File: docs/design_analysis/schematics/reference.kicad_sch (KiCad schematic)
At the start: 0 parts

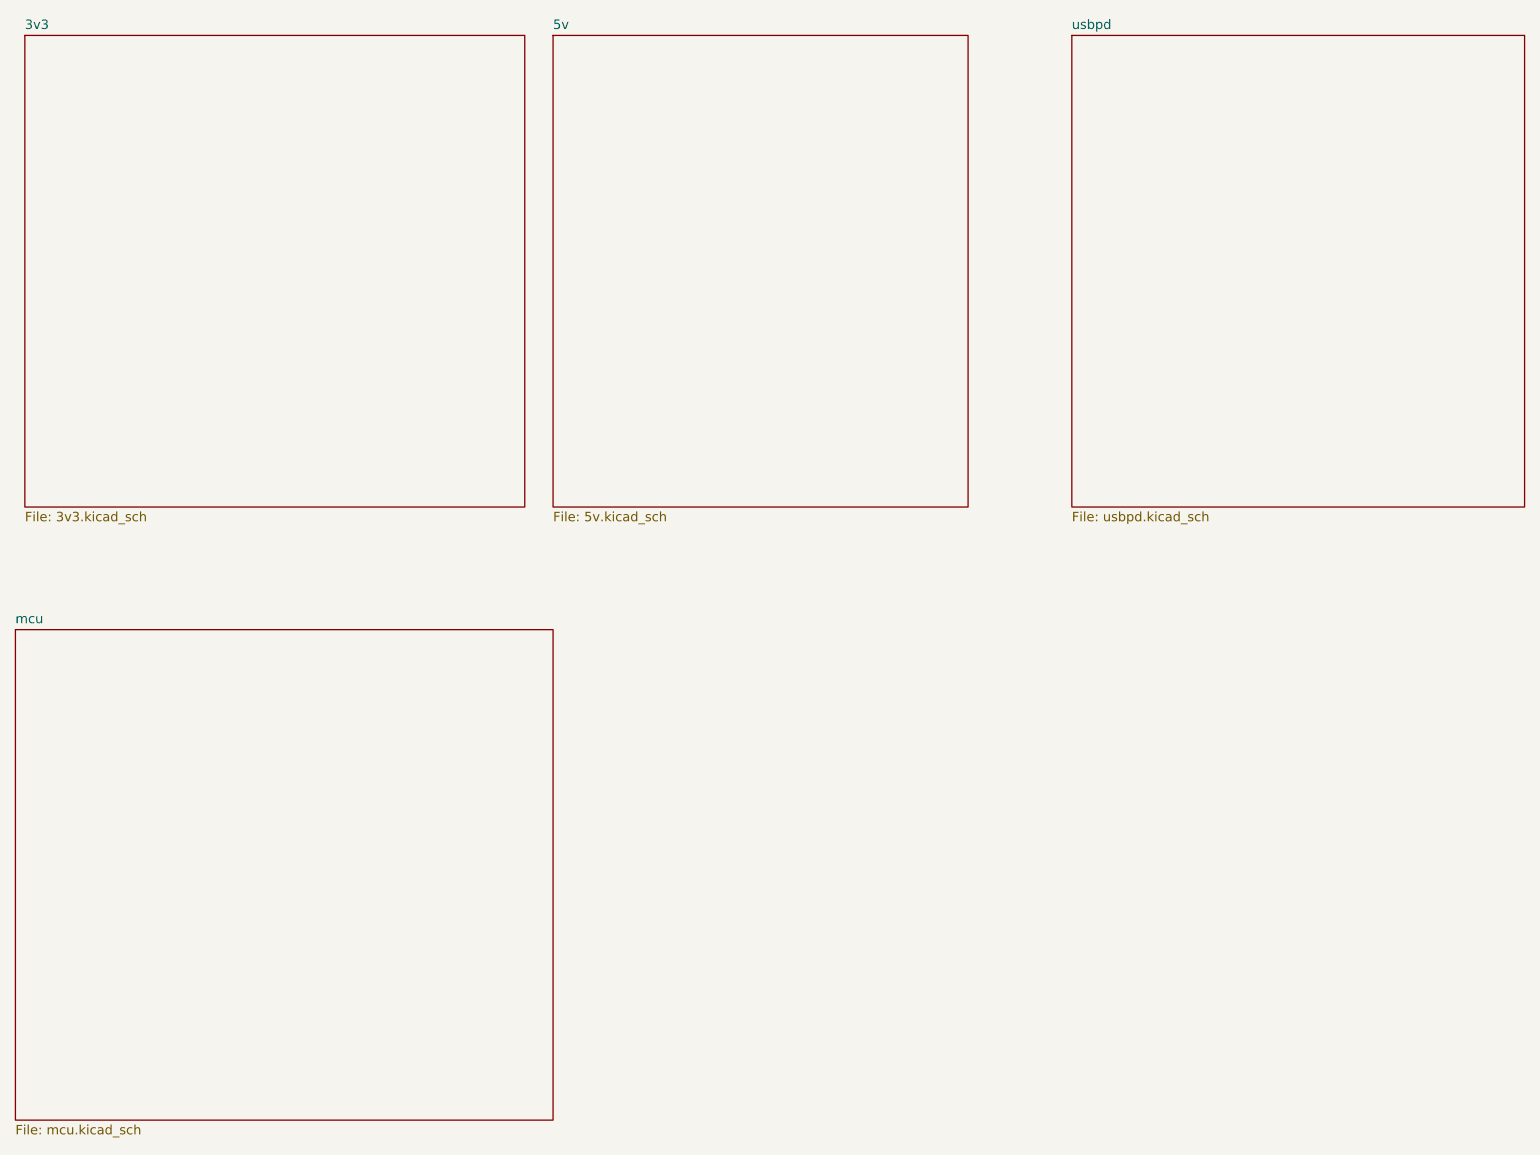
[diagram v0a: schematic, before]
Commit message: HV converter Rev C redesign around LM5156
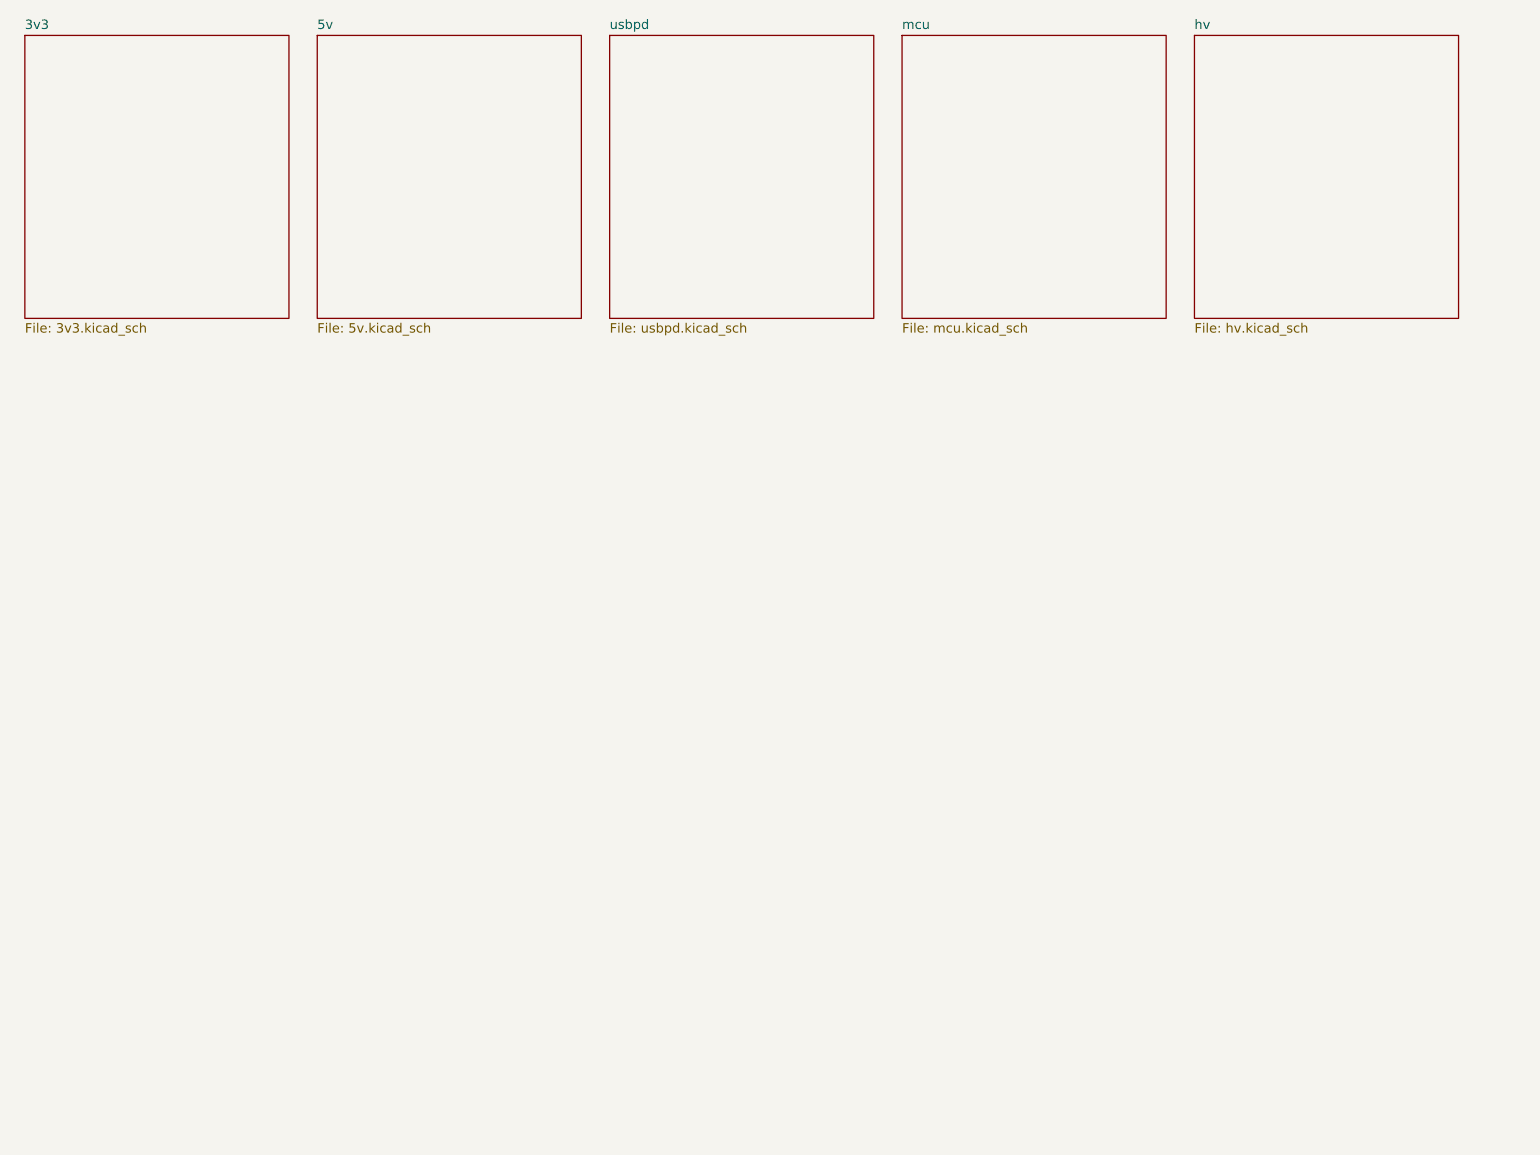
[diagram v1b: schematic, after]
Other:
- added sheet hv (hv.kicad_sch)
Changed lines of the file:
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@@
 (kicad_sch
-	(version 20250114)
+	(version 20260306)
 	(generator "eeschema")
-	(generator_version "9.0")
+	(generator_version "10.0")
 	(paper "A4")
 	(sheet
-		(at 99.06 24.13)
-		(size 55.88 63.5)
-		(exclude_from_sim no)
-		(in_bom yes)
-		(on_board yes)
-		(dnp no)
-		(fields_autoplaced yes)
-		(stroke
-			(width 0.1524)
-			(type solid)
-		)
-		(fill
-			(color 0 0 0 0.0000)
+		(at 67.31 24.13)
+		(size 35.56 38.1)
+		(exclude_from_sim no)
+		(in_bom yes)
+		(on_board yes)
+		(dnp no)
+		(fields_autoplaced yes)
+		(stroke
+			(width 0.1524)
+			(type solid)
+		)
+		(fill
+			(color 0 0 0 0)
 		)
 		(property "Sheetname" "5v"
-			(at 99.06 23.4184 0)
+			(at 67.31 23.4184 0)
+			(show_name no)
+			(do_not_autoplace no)
 			(effects
 				(font
@@
 		)
 		(property "Sheetfile" "5v.kicad_sch"
-			(at 99.06 88.2146 0)
+			(at 67.31 62.8146 0)
+			(show_name no)
+			(do_not_autoplace no)
 			(effects
 				(font
@@
 	(sheet
 		(at 27.94 24.13)
-		(size 67.31 63.5)
-		(exclude_from_sim no)
-		(in_bom yes)
-		(on_board yes)
-		(dnp no)
-		(fields_autoplaced yes)
-		(stroke
-			(width 0.1524)
-			(type solid)
-		)
-		(fill
-			(color 0 0 0 0.0000)
+		(size 35.56 38.1)
+		(exclude_from_sim no)
+		(in_bom yes)
+		(on_board yes)
+		(dnp no)
+		(fields_autoplaced yes)
+		(stroke
+			(width 0.1524)
+			(type solid)
+		)
+		(fill
+			(color 0 0 0 0)
 		)
 		(property "Sheetname" "3v3"
 			(at 27.94 23.4184 0)
+			(show_name no)
+			(do_not_autoplace no)
 			(effects
 				(font
@@
 		)
 		(property "Sheetfile" "3v3.kicad_sch"
-			(at 27.94 88.2146 0)
+			(at 27.94 62.8146 0)
+			(show_name no)
+			(do_not_autoplace no)
 			(effects
 				(font
@@
 	)
 	(sheet
-		(at 26.67 104.14)
-		(size 72.39 66.04)
-		(exclude_from_sim no)
-		(in_bom yes)
-		(on_board yes)
-		(dnp no)
-		(fields_autoplaced yes)
-		(stroke
-			(width 0.1524)
-			(type solid)
-		)
-		(fill
-			(color 0 0 0 0.0000)
+		(at 146.05 24.13)
+		(size 35.56 38.1)
+		(exclude_from_sim no)
+		(in_bom yes)
+		(on_board yes)
+		(dnp no)
+		(fields_autoplaced yes)
+		(stroke
+			(width 0.1524)
+			(type solid)
+		)
+		(fill
+			(color 0 0 0 0)
 		)
 		(property "Sheetname" "mcu"
-			(at 26.67 103.4284 0)
+			(at 146.05 23.4184 0)
+			(show_name no)
+			(do_not_autoplace no)
 			(effects
 				(font
@@
 		)
 		(property "Sheetfile" "mcu.kicad_sch"
-			(at 26.67 170.7646 0)
+			(at 146.05 62.8146 0)
+			(show_name no)
+			(do_not_autoplace no)
 			(effects
 				(font
@@
 	)
 	(sheet
-		(at 168.91 24.13)
-		(size 60.96 63.5)
-		(exclude_from_sim no)
-		(in_bom yes)
-		(on_board yes)
-		(dnp no)
-		(fields_autoplaced yes)
-		(stroke
-			(width 0.1524)
-			(type solid)
-		)
-		(fill
-			(color 0 0 0 0.0000)
+		(at 106.68 24.13)
+		(size 35.56 38.1)
+		(exclude_from_sim no)
+		(in_bom yes)
+		(on_board yes)
+		(dnp no)
+		(fields_autoplaced yes)
+		(stroke
+			(width 0.1524)
+			(type solid)
+		)
+		(fill
+			(color 0 0 0 0)
 		)
 		(property "Sheetname" "usbpd"
-			(at 168.91 23.4184 0)
+			(at 106.68 23.4184 0)
+			(show_name no)
+			(do_not_autoplace no)
 			(effects
 				(font
@@
 		)
 		(property "Sheetfile" "usbpd.kicad_sch"
-			(at 168.91 88.2146 0)
+			(at 106.68 62.8146 0)
+			(show_name no)
+			(do_not_autoplace no)
 			(effects
 				(font
@@
 				)
 			)
+		)
+	)
+	(sheet
+		(at 185.42 24.13)
+		(size 35.56 38.1)
+		(exclude_from_sim no)
+		(in_bom yes)
+		(on_board yes)
+		(dnp no)
+		(fields_autoplaced yes)
+		(stroke
+			(width 0.1524)
+			(type solid)
+		)
+		(fill
+			(color 0 0 0 0)
+		)
+		(property "Sheetname" "hv"
+			(at 185.42 23.4184 0)
+			(show_name no)
+			(do_not_autoplace no)
+			(effects
+				(font
+					(size 1.27 1.27)
+				)
+				(justify left bottom)
+			)
+		)
+		(property "Sheetfile" "hv.kicad_sch"
+			(at 185.42 62.8146 0)
+			(show_name no)
+			(do_not_autoplace no)
+			(effects
+				(font
+					(size 1.27 1.27)
+				)
+				(justify left top)
+			)
+		)
+		(instances
+			(project "reference"
+				(path "/12d1c5ca-8caa-430e-acde-de5e63359dde"
+					(page "6")
+				)
+			)
